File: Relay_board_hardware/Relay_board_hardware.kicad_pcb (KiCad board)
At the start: 2 copper layers, 101.6 x 101.6 mm, 24 parts, among them IC1 BTS3800SL, Q1 IRF740ASPBF, U1 AD8541, U2 MCP1416

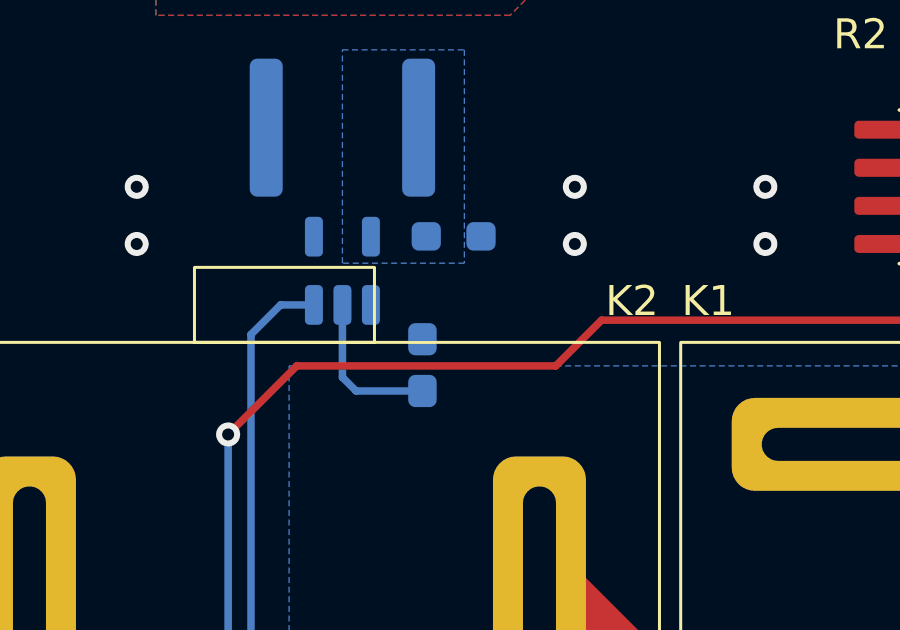
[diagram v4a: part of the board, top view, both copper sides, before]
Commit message: added filter cap, changed opamp datasheet
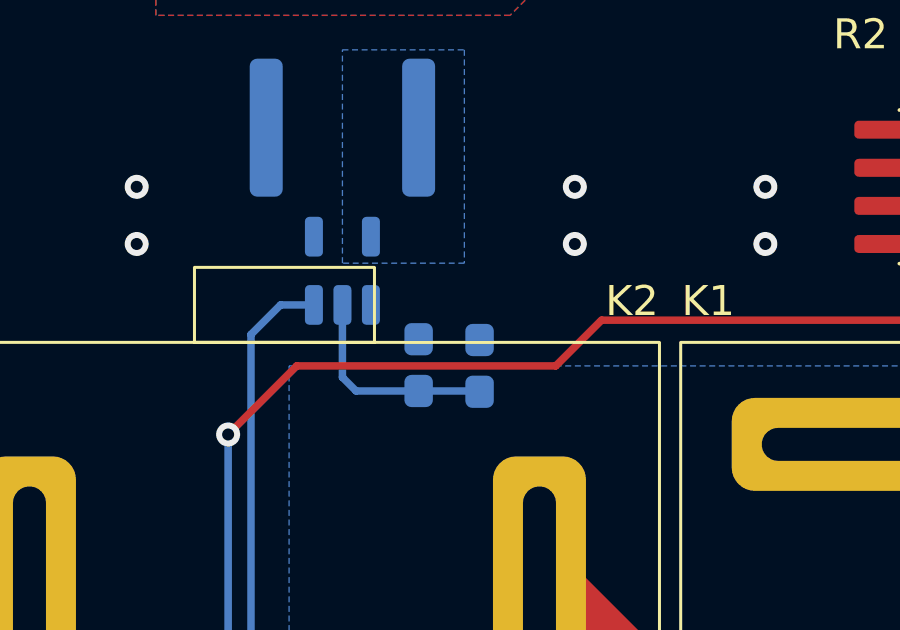
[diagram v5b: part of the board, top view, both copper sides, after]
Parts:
- removed R3: 10k, Resistor_SMD:R_0603_1608Metric_Pad0.98x0.95mm_HandSolder
- added C2: 0.1u, Capacitor_SMD:C_0603_1608Metric_Pad1.08x0.95mm_HandSolder, B.Cu at (146.1, 103.1)
- moved C1 0.13 mm to (144.0, 103.1)
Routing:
- net +12V: track 21.0 -> 23.1 mm
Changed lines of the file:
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@@
       (net 7 "/PWRRES") (pinfunction "1") (pintype "input") (zone_connect 2))
-  )
-  (footprint "Resistor_SMD:R_0603_1608Metric_Pad0.98x0.95mm_HandSolder" (layer "B.Cu")
-    (at 145.1845 98.806 180)
-    (descr "Resistor SMD 0603 (1608 Metric), square (rectangular) end terminal, IPC_7351 nominal with elongated pad for handsoldering. (Body size source: IPC-SM-782 page 72, https://www.pcb-3d.com/wordpress/wp-content/uploads/ipc-sm-782a_amendment_1_and_2.pdf), generated with kicad-footprint-generator")
-    (tags "resistor handsolder")
-    (property "Price" "0.37")
-    (property "Sheetfile" "Relay_board_hardware.kicad_sch")
-    (property "Sheetname" "")
-    (property "ki_description" "Resistor")
-    (property "ki_keywords" "R res resistor")
-    (attr smd)
-    (fp_text reference "R3" (at -2.8975 0) (layer "B.SilkS")
-        (effects (font (size 1 1) (thickness 0.15)) (justify mirror))
-    )
-    (fp_text value "10k" (at 0 -1.43) (layer "B.Fab")
-        (effects (font (size 1 1) (thickness 0.15)) (justify mirror))
-    )
-    (fp_text user "${REFERENCE}" (at 0 0) (layer "B.Fab")
-        (effects (font (size 0.4 0.4) (thickness 0.06)) (justify mirror))
-    )
-    (fp_line (start -0.254724 -0.5225) (end 0.254724 -0.5225)
-      (stroke (width 0.12) (type solid)) (layer "B.SilkS"))
-    (fp_line (start -0.254724 0.5225) (end 0.254724 0.5225)
-      (stroke (width 0.12) (type solid)) (layer "B.SilkS"))
-    (fp_line (start -1.65 -0.73) (end -1.65 0.73)
-      (stroke (width 0.05) (type solid)) (layer "B.CrtYd"))
-    (fp_line (start -1.65 0.73) (end 1.65 0.73)
-      (stroke (width 0.05) (type solid)) (layer "B.CrtYd"))
-    (fp_line (start 1.65 -0.73) (end -1.65 -0.73)
-      (stroke (width 0.05) (type solid)) (layer "B.CrtYd"))
-    (fp_line (start 1.65 0.73) (end 1.65 -0.73)
-      (stroke (width 0.05) (type solid)) (layer "B.CrtYd"))
-    (fp_line (start -0.8 -0.4125) (end -0.8 0.4125)
-      (stroke (width 0.1) (type solid)) (layer "B.Fab"))
-    (fp_line (start -0.8 0.4125) (end 0.8 0.4125)
-      (stroke (width 0.1) (type solid)) (layer "B.Fab"))
-    (fp_line (start 0.8 -0.4125) (end -0.8 -0.4125)
-      (stroke (width 0.1) (type solid)) (layer "B.Fab"))
-    (fp_line (start 0.8 0.4125) (end 0.8 -0.4125)
-      (stroke (width 0.1) (type solid)) (layer "B.Fab"))
-    (pad "1" smd roundrect (at -0.9125 0 180) (size 0.975 0.95) (layers "B.Cu" "B.Paste" "B.Mask") (roundrect_rratio 0.25)
-      (net 1 "GND") (pintype "passive"))
-    (pad "2" smd roundrect (at 0.9125 0 180) (size 0.975 0.95) (layers "B.Cu" "B.Paste" "B.Mask") (roundrect_rratio 0.25)
-      (net 13 "Net-(Q1-G)") (pintype "passive"))
-    (model "${KICAD6_3DMODEL_DIR}/Resistor_SMD.3dshapes/R_0603_1608Metric.wrl"
-      (offset (xyz 0 0 0))
-      (scale (xyz 1 1 1))
-      (rotate (xyz 0 0 0))
-    )
   )
   (footprint "Symbol:Symbol_HighVoltage_Type2_CopperTop_VerySmall" (layer "B.Cu")
@@
   )
   (footprint "Capacitor_SMD:C_0603_1608Metric_Pad1.08x0.95mm_HandSolder" (layer "B.Cu")
-    (at 144.145 103.0975 90)
+    (at 144.018 103.0975 90)
     (descr "Capacitor SMD 0603 (1608 Metric), square (rectangular) end terminal, IPC_7351 nominal with elongated pad for handsoldering. (Body size source: IPC-SM-782 page 76, https://www.pcb-3d.com/wordpress/wp-content/uploads/ipc-sm-782a_amendment_1_and_2.pdf), generated with kicad-footprint-generator")
     (tags "capacitor handsolder")
@@
     (property "ki_keywords" "cap capacitor")
     (attr smd)
-    (fp_text reference "C1" (at 0 1.43 90) (layer "B.SilkS")
+    (fp_text reference "C1" (at 2.5135 0 90) (layer "B.SilkS")
         (effects (font (size 1 1) (thickness 0.15)) (justify mirror))
     )
@@
     (fp_line (start 4.699 -2.794) (end -4.699 -2.794)
       (stroke (width 0.381) (type solid)) (layer "B.Cu"))
+  )
+  (footprint "Capacitor_SMD:C_0603_1608Metric_Pad1.08x0.95mm_HandSolder" (layer "B.Cu")
+    (at 146.05 103.124 90)
+    (descr "Capacitor SMD 0603 (1608 Metric), square (rectangular) end terminal, IPC_7351 nominal with elongated pad for handsoldering. (Body size source: IPC-SM-782 page 76, https://www.pcb-3d.com/wordpress/wp-content/uploads/ipc-sm-782a_amendment_1_and_2.pdf), generated with kicad-footprint-generator")
+    (tags "capacitor handsolder")
+    (property "Sheetfile" "Relay_board_hardware.kicad_sch")
+    (property "Sheetname" "")
+    (property "ki_description" "Unpolarized capacitor")
+    (property "ki_keywords" "cap capacitor")
+    (attr smd)
+    (fp_text reference "C2" (at 2.54 0 90) (layer "B.SilkS")
+        (effects (font (size 1 1) (thickness 0.15)) (justify mirror))
+    )
+    (fp_text value "0.1u" (at 0 -1.43 90) (layer "B.Fab")
+        (effects (font (size 1 1) (thickness 0.15)) (justify mirror))
+    )
+    (fp_text user "${REFERENCE}" (at 0 0 90) (layer "B.Fab")
+        (effects (font (size 0.4 0.4) (thickness 0.06)) (justify mirror))
+    )
+    (fp_line (start -0.146267 -0.51) (end 0.146267 -0.51)
+      (stroke (width 0.12) (type solid)) (layer "B.SilkS"))
+    (fp_line (start -0.146267 0.51) (end 0.146267 0.51)
+      (stroke (width 0.12) (type solid)) (layer "B.SilkS"))
+    (fp_line (start -1.65 -0.73) (end -1.65 0.73)
+      (stroke (width 0.05) (type solid)) (layer "B.CrtYd"))
+    (fp_line (start -1.65 0.73) (end 1.65 0.73)
+      (stroke (width 0.05) (type solid)) (layer "B.CrtYd"))
+    (fp_line (start 1.65 -0.73) (end -1.65 -0.73)
+      (stroke (width 0.05) (type solid)) (layer "B.CrtYd"))
+    (fp_line (start 1.65 0.73) (end 1.65 -0.73)
+      (stroke (width 0.05) (type solid)) (layer "B.CrtYd"))
+    (fp_line (start -0.8 -0.4) (end -0.8 0.4)
+      (stroke (width 0.1) (type solid)) (layer "B.Fab"))
+    (fp_line (start -0.8 0.4) (end 0.8 0.4)
+      (stroke (width 0.1) (type solid)) (layer "B.Fab"))
+    (fp_line (start 0.8 -0.4) (end -0.8 -0.4)
+      (stroke (width 0.1) (type solid)) (layer "B.Fab"))
+    (fp_line (start 0.8 0.4) (end 0.8 -0.4)
+      (stroke (width 0.1) (type solid)) (layer "B.Fab"))
+    (pad "1" smd roundrect (at -0.8625 0 90) (size 1.075 0.95) (layers "B.Cu" "B.Paste" "B.Mask") (roundrect_rratio 0.25)
+      (net 12 "+12V") (pintype "passive"))
+    (pad "2" smd roundrect (at 0.8625 0 90) (size 1.075 0.95) (layers "B.Cu" "B.Paste" "B.Mask") (roundrect_rratio 0.25)
+      (net 1 "GND") (pintype "passive"))
+    (model "${KICAD6_3DMODEL_DIR}/Capacitor_SMD.3dshapes/C_0603_1608Metric.wrl"
+      (offset (xyz 0 0 0))
+      (scale (xyz 1 1 1))
+      (rotate (xyz 0 0 0))
+    )
   )
   (footprint "MRDT_Silkscreens:yagi2_20mm" (layer "B.Cu")
@@
   (segment (start 141.478 101.092) (end 141.478 103.505) (width 0.25) (layer "B.Cu") (net 12))
   (segment (start 140.97 128.905) (end 140.97 139.192) (width 2.54) (layer "B.Cu") (net 12))
+  (segment (start 144.018 103.96) (end 146.0235 103.96) (width 0.25) (layer "B.Cu") (net 12))
+  (segment (start 146.0235 103.96) (end 146.05 103.9865) (width 0.25) (layer "B.Cu") (net 12))
   (zone (net 3) (net_name "VBUS") (layer "F.Cu") (hatch edge 0.5)
     (priority 6)
